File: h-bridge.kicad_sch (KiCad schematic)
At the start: 20 parts, among them J5 Conn_02x06_Counter_Clockwise, M3 DC, Q10 Q_NMOS, Q7 Q_NMOS, Q8 Q_NMOS, Q9 Q_NMOS, U11 DRV8701

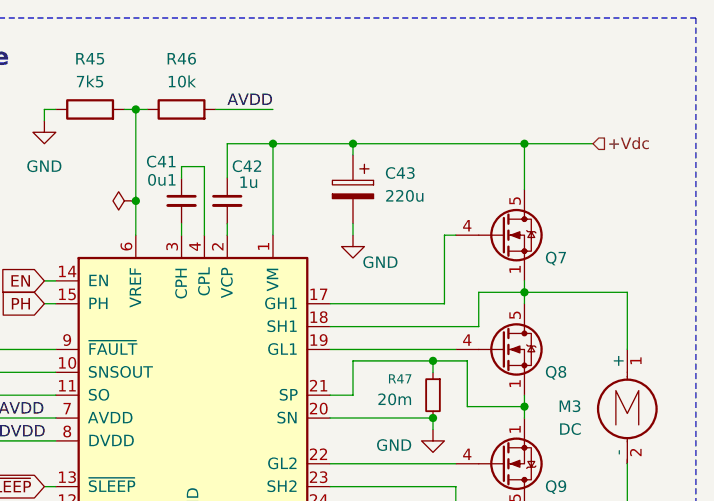
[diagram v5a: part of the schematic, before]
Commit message: schem: add 0u1 decoupling cap to DRV8701
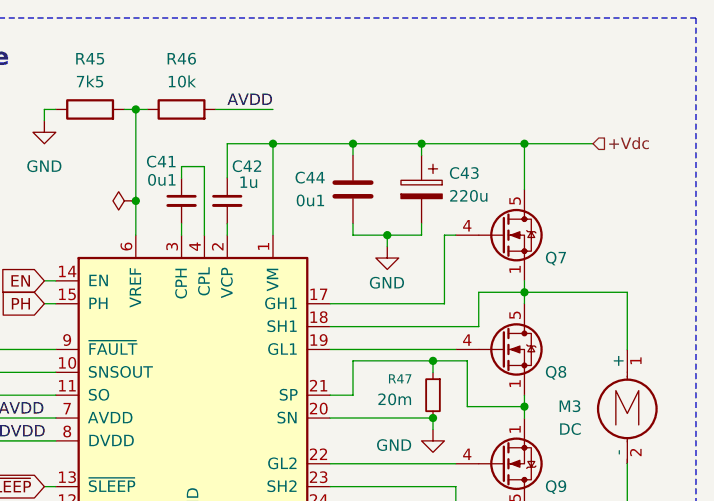
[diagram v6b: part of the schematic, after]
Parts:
- added C44: 0u1, Capacitor_SMD:C_0402_1005Metric, symbol Device:C
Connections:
- net +Vdc: now also C44.1
- net GND: now also C44.2
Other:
- moved on the sheet: C43
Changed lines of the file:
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@@
 	)
 	(junction
+		(at 165.1 58.42)
+		(diameter 0)
+		(color 0 0 0 0)
+	)
+	(junction
+		(at 168.91 68.58)
+		(diameter 0)
+		(color 0 0 0 0)
+	)
+	(junction
 		(at 111.76 120.65)
 		(diameter 0)
@@
 	)
 	(junction
-		(at 165.1 58.42)
-		(diameter 0)
-		(color 0 0 0 0)
-	)
-	(junction
 		(at 140.97 64.77)
 		(diameter 0)
@@
 		(color 0 0 0 0)
 	)
+	(junction
+		(at 172.72 58.42)
+		(diameter 0)
+		(color 0 0 0 0)
+	)
 	(no_connect
 		(at 127 116.84)
@@
 	(wire
 		(pts
+			(xy 172.72 68.58) (xy 172.72 67.31)
+		)
+		(stroke
+			(width 0)
+			(type default)
+		)
+	)
+	(wire
+		(pts
 			(xy 148.59 68.58) (xy 148.59 60.96)
 		)
@@
 	(wire
 		(pts
+			(xy 165.1 58.42) (xy 165.1 59.69)
+		)
+		(stroke
+			(width 0)
+			(type default)
+		)
+	)
+	(wire
+		(pts
 			(xy 130.81 73.66) (xy 132.08 73.66)
 		)
@@
 	(wire
 		(pts
+			(xy 165.1 58.42) (xy 172.72 58.42)
+		)
+		(stroke
+			(width 0)
+			(type default)
+		)
+	)
+	(wire
+		(pts
 			(xy 184.15 73.66) (xy 184.15 74.93)
 		)
@@
 	(wire
 		(pts
-			(xy 165.1 67.31) (xy 165.1 68.58)
+			(xy 168.91 68.58) (xy 168.91 69.85)
 		)
 		(stroke
@@
 	(wire
 		(pts
+			(xy 172.72 58.42) (xy 184.15 58.42)
+		)
+		(stroke
+			(width 0)
+			(type default)
+		)
+	)
+	(wire
+		(pts
 			(xy 179.07 78.74) (xy 179.07 74.93)
 		)
@@
 	(wire
 		(pts
+			(xy 165.1 68.58) (xy 165.1 67.31)
+		)
+		(stroke
+			(width 0)
+			(type default)
+		)
+	)
+	(wire
+		(pts
 			(xy 130.81 76.2) (xy 132.08 76.2)
 		)
@@
 	(wire
 		(pts
-			(xy 165.1 58.42) (xy 184.15 58.42)
+			(xy 110.49 101.6) (xy 110.49 102.87)
 		)
 		(stroke
@@
 	(wire
 		(pts
-			(xy 110.49 101.6) (xy 110.49 102.87)
+			(xy 172.72 58.42) (xy 172.72 59.69)
 		)
 		(stroke
@@
 	(wire
 		(pts
-			(xy 165.1 58.42) (xy 165.1 59.69)
+			(xy 168.91 68.58) (xy 165.1 68.58)
 		)
 		(stroke
@@
 	(wire
 		(pts
+			(xy 168.91 68.58) (xy 172.72 68.58)
+		)
+		(stroke
+			(width 0)
+			(type default)
+		)
+	)
+	(wire
+		(pts
 			(xy 162.56 93.98) (xy 176.53 93.98)
 		)
@@
 	(symbol
 		(lib_id "Device:C_Polarized")
-		(at 165.1 63.5 0)
+		(at 172.72 63.5 0)
 		(mirror y)
 		(unit 1)
@@
 		(dnp no)
 		(property "Reference" "C43"
-			(at 168.656 61.722 0)
+			(at 175.768 61.722 0)
 			(effects
 				(font
@@
 		)
 		(property "Value" "220u"
-			(at 168.656 64.262 0)
+			(at 175.768 64.262 0)
 			(effects
 				(font
@@
 		)
 		(property "Footprint" "Capacitor_SMD:CP_Elec_6.3x7.7"
-			(at 164.1348 67.31 0)
+			(at 171.7548 67.31 0)
 			(effects
 				(font
@@
 		)
 		(property "Datasheet" "~"
-			(at 165.1 63.5 0)
+			(at 172.72 63.5 0)
 			(effects
 				(font
@@
 		)
 		(property "Description" "Polarized capacitor"
-			(at 165.1 63.5 0)
+			(at 172.72 63.5 0)
 			(effects
 				(font
@@
 		)
 		(property "Basic" "X"
-			(at 165.1 63.5 0)
+			(at 172.72 63.5 0)
 			(effects
 				(font
@@
 		)
 		(property "JLCPCB Part #" "C46550411"
-			(at 165.1 63.5 0)
+			(at 172.72 63.5 0)
 			(effects
 				(font
@@
 		)
 		(property "Manufacturer" "jieerrui"
-			(at 165.1 63.5 0)
+			(at 172.72 63.5 0)
 			(effects
 				(font
@@
 		)
 		(property "Manufacturer Part Number" "JVJ35V220M6x8"
-			(at 165.1 63.5 0)
+			(at 172.72 63.5 0)
 			(effects
 				(font
@@
 	)
 	(symbol
+		(lib_id "Device:C")
+		(at 165.1 63.5 0)
+		(mirror y)
+		(unit 1)
+		(exclude_from_sim no)
+		(in_bom yes)
+		(on_board yes)
+		(dnp no)
+		(property "Reference" "C44"
+			(at 162.052 62.23 0)
+			(effects
+				(font
+					(size 1.27 1.27)
+				)
+				(justify left)
+			)
+		)
+		(property "Value" "0u1"
+			(at 162.052 64.77 0)
+			(effects
+				(font
+					(size 1.27 1.27)
+				)
+				(justify left)
+			)
+		)
+		(property "Footprint" "Capacitor_SMD:C_0402_1005Metric"
+			(at 164.1348 67.31 0)
+			(effects
+				(font
+					(size 1.27 1.27)
+				)
+				(hide yes)
+			)
+		)
+		(property "Datasheet" "~"
+			(at 165.1 63.5 0)
+			(effects
+				(font
+					(size 1.27 1.27)
+				)
+				(hide yes)
+			)
+		)
+		(property "Description" "Unpolarized capacitor"
+			(at 165.1 63.5 0)
+			(effects
+				(font
+					(size 1.27 1.27)
+				)
+				(hide yes)
+			)
+		)
+		(property "Manufacturer" "Samsung Electro-Mechanics "
+			(at 165.1 63.5 0)
+			(effects
+				(font
+					(size 1.27 1.27)
+				)
+				(hide yes)
+			)
+		)
+		(property "Manufacturer Part Number" "CL05B104KB54PNC"
+			(at 165.1 63.5 0)
+			(effects
+				(font
+					(size 1.27 1.27)
+				)
+				(hide yes)
+			)
+		)
+		(property "Basic" "Y"
+			(at 165.1 63.5 0)
+			(effects
+				(font
+					(size 1.27 1.27)
+				)
+				(hide yes)
+			)
+		)
+		(property "JLCPCB Part #" "C307331"
+			(at 165.1 63.5 0)
+			(effects
+				(font
+					(size 1.27 1.27)
+				)
+				(hide yes)
+			)
+		)
+		(pin "1"
+		)
+		(pin "2"
+		)
+		(instances
+			(project "motor-power-poc"
+				(path "/a1dc4c9e-7b20-4b66-a693-9133bc644c6b/234f18ec-899d-4a38-bb51-5ceaab0ae171"
+					(reference "C44")
+					(unit 1)
+				)
+			)
+		)
+	)
+	(symbol
 		(lib_id "Device:R")
 		(at 118.11 76.2 0)
@@
 	(symbol
 		(lib_id "power:GND")
-		(at 165.1 68.58 0)
+		(at 168.91 69.85 0)
 		(unit 1)
 		(exclude_from_sim no)
@@
 		(dnp no)
 		(property "Reference" "#PWR087"
-			(at 165.1 74.93 0)
+			(at 168.91 76.2 0)
 			(effects
 				(font
@@
 		)
 		(property "Value" "GND"
-			(at 168.148 71.628 0)
+			(at 166.878 73.914 0)
 			(effects
 				(font
 					(size 1.27 1.27)
 				)
+				(justify left)
 			)
 		)
 		(property "Footprint" ""
-			(at 165.1 68.58 0)
+			(at 168.91 69.85 0)
 			(effects
 				(font
@@
 		)
 		(property "Datasheet" ""
-			(at 165.1 68.58 0)
+			(at 168.91 69.85 0)
 			(effects
 				(font
@@
 		)
 		(property "Description" "Power symbol creates a global label with name \"GND\" , ground"
-			(at 165.1 68.58 0)
+			(at 168.91 69.85 0)
 			(effects
 				(font

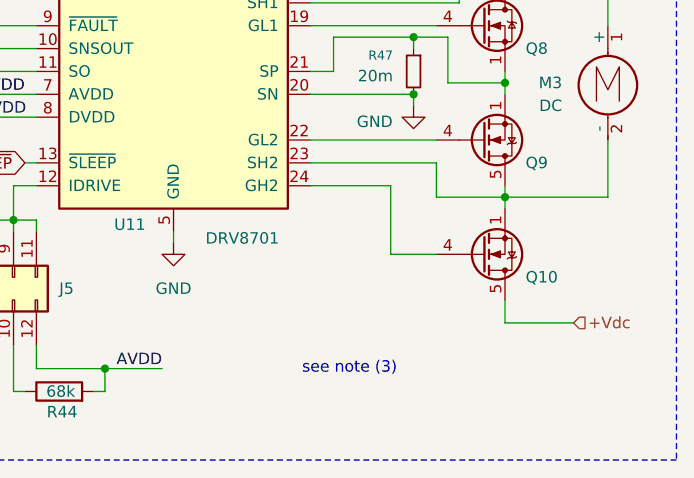
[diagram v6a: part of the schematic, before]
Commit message: schem: add DRV8701 gate test point
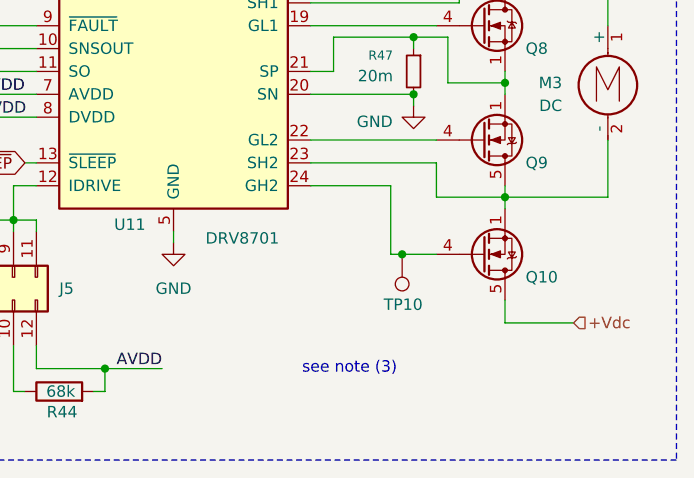
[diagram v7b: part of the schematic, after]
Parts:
- added TP10: TestPoint, GLCS:TestPoint_Keystone_5015_Micro_Mini, symbol Connector:TestPoint
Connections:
- net at Q10.4 (G), U11.24 (GH2): now also TP10.1
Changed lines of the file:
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@@
 	)
 	(junction
+		(at 172.72 106.68)
+		(diameter 0)
+		(color 0 0 0 0)
+	)
+	(junction
 		(at 172.72 58.42)
 		(diameter 0)
@@
 	(wire
 		(pts
-			(xy 171.45 106.68) (xy 176.53 106.68)
+			(xy 171.45 106.68) (xy 172.72 106.68)
 		)
 		(stroke
@@
 	(wire
 		(pts
+			(xy 172.72 106.68) (xy 176.53 106.68)
+		)
+		(stroke
+			(width 0)
+			(type default)
+		)
+	)
+	(wire
+		(pts
 			(xy 175.26 76.2) (xy 162.56 76.2)
 		)
@@
 					(unit 1)
 				)
+			)
+		)
+	)
+	(symbol
+		(lib_id "Connector:TestPoint")
+		(at 172.72 106.68 180)
+		(unit 1)
+		(exclude_from_sim no)
+		(in_bom yes)
+		(on_board yes)
+		(dnp no)
+		(property "Reference" "TP10"
+			(at 175.006 112.268 0)
+			(effects
+				(font
+					(size 1.27 1.27)
+				)
+				(justify left)
+			)
+		)
+		(property "Value" "TestPoint"
+			(at 170.18 108.7121 0)
+			(effects
+				(font
+					(size 1.27 1.27)
+				)
+				(justify left)
+				(hide yes)
+			)
+		)
+		(property "Footprint" "GLCS:TestPoint_Keystone_5015_Micro_Mini"
+			(at 167.64 106.68 0)
+			(effects
+				(font
+					(size 1.27 1.27)
+				)
+				(hide yes)
+			)
+		)
+		(property "Datasheet" "~"
+			(at 167.64 106.68 0)
+			(effects
+				(font
+					(size 1.27 1.27)
+				)
+				(hide yes)
+			)
+		)
+		(property "Description" "test point"
+			(at 172.72 106.68 0)
+			(effects
+				(font
+					(size 1.27 1.27)
+				)
+				(hide yes)
+			)
+		)
+		(property "Basic" "X"
+			(at 172.72 106.68 0)
+			(effects
+				(font
+					(size 1.27 1.27)
+				)
+				(hide yes)
+			)
+		)
+		(property "JLCPCB Part #" "C2906768"
+			(at 172.72 106.68 0)
+			(effects
+				(font
+					(size 1.27 1.27)
+				)
+				(hide yes)
+			)
+		)
+		(property "Manufacturer" "Keystone"
+			(at 172.72 106.68 0)
+			(effects
+				(font
+					(size 1.27 1.27)
+				)
+				(hide yes)
+			)
+		)
+		(property "Manufacturer Part Number" "5015"
+			(at 172.72 106.68 0)
+			(effects
+				(font
+					(size 1.27 1.27)
+				)
+				(hide yes)
+			)
+		)
+		(pin "1"
+		)
+		(instances
+			(project "motor-power-poc"
+				(path "/a1dc4c9e-7b20-4b66-a693-9133bc644c6b/234f18ec-899d-4a38-bb51-5ceaab0ae171"
+					(reference "TP10")
+					(unit 1)
+				)
